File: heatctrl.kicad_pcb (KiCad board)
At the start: 4 copper layers, 57 x 55.5 mm, 6 parts, among them J1 Conn_01x10_Pin, U1 T-Display-S3

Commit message: mcp and t-display-s3
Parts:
- removed J1: Conn_01x10_Pin, Connector_PinSocket_2.54mm:PinSocket_1x10_P2.54mm_Vertical
- removed REF** (x4): MountingHole_3.2mm_M3_Pad, MountingHole:MountingHole_3.2mm_M3_Pad
- added J2: Conn_01x10_Socket, Connector_PinSocket_2.54mm:PinSocket_1x10_P2.54mm_Vertical, F.Cu at (145.4, 74.9)
- added U2: MCP23017_SS, Package_SO:SSOP-28_5.3x10.2mm_P0.65mm, F.Cu at (157.5, 99.1)
- moved U1 20.1 mm to (217.5, 87.6)
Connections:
- U1 pad 1: unconnected-(U1-3v-Pad1) -> +3V3
- U1 pad 11: unconnected-(U1-GND-Pad11) -> GND
- U1 pad 12: unconnected-(U1-5V-Pad12) -> +5V
- U1 pad 17: unconnected-(U1-18-Pad17) -> SCL
- U1 pad 18: Net-(J1-Pin_8) -> SDA
- U1 pad 2: Net-(J1-Pin_2) -> unconnected-(U1-1-Pad2)
- U1 pad 20: Net-(J1-Pin_7) -> unconnected-(U1-16-Pad20)
- U1 pad 24: Net-(J1-Pin_10) -> +3V3
- U1 pad 3: Net-(J1-Pin_3) -> unconnected-(U1-2-Pad3)
- U1 pad 6: Net-(J1-Pin_4) -> unconnected-(U1-11-Pad6)
- U1 pad 7: Net-(J1-Pin_5) -> unconnected-(U1-12-Pad7)
- U1 pad 8: Net-(J1-Pin_6) -> RESET
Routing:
- net Net-(J1-Pin_8): track 82.2 -> 0.00 mm
- net Net-(J1-Pin_7): track 59.6 -> 0.00 mm
- net Net-(J1-Pin_10): track 46.3 -> 0.00 mm
- net Net-(J1-Pin_6): track 10.2 -> 0.00 mm
- net Net-(J1-Pin_5): track 10.2 -> 0.00 mm
- net Net-(J1-Pin_4): track 10.2 -> 0.00 mm
- net Net-(J1-Pin_3): track 10.0 -> 0.00 mm
- net Net-(J1-Pin_2): track 10.0 -> 0.00 mm
- removed copper zone on F.Cu, net GND
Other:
- board outline removed
- board text removed: "AC1"
- board text removed: "AC2"
- board text removed: "AC3"
- board text removed: "AC4"
- board text removed: "AC5"
- board text removed: "AC6"
- board text removed: "AC7"
- board text removed: "GND"
- board text removed: "Heat Controller"
- board text removed: "V1.0 Heiko Vogeler 2026-01-07"

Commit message: start pcb
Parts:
- added D1: Yellow, PCM_JLCPCB:D_0805, F.Cu at (196.2, 77.8)
- added D7: Red, PCM_JLCPCB:D_0805, F.Cu at (200.7, 77.8)
- added J1: Conn_01x10_Socket, Connector_PinSocket_2.54mm:PinSocket_1x10_P2.54mm_Vertical, F.Cu at (168.3, 81.3)
- added R1: 470, Resistor_SMD:R_0603_1608Metric, F.Cu at (196.2, 81.7)
- added R11: 470, Resistor_SMD:R_0603_1608Metric, F.Cu at (200.7, 81.7)
- moved J2 42.5 mm to (145.4, 117.5)
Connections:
- J2 pad 1: unconnected-(J2-Pin_1-Pad1) -> +5V
- J2 pad 10: unconnected-(J2-Pin_10-Pad10) -> GND
- J2 pad 2: unconnected-(J2-Pin_2-Pad2) -> Net-(J2-Pin_2)
- J2 pad 3: unconnected-(J2-Pin_3-Pad3) -> Net-(J2-Pin_3)
- J2 pad 4: unconnected-(J2-Pin_4-Pad4) -> Net-(J2-Pin_4)
- J2 pad 5: unconnected-(J2-Pin_5-Pad5) -> Net-(J2-Pin_5)
- J2 pad 6: unconnected-(J2-Pin_6-Pad6) -> Net-(J2-Pin_6)
- J2 pad 7: unconnected-(J2-Pin_7-Pad7) -> Net-(J2-Pin_7)
- J2 pad 8: unconnected-(J2-Pin_8-Pad8) -> Net-(J2-Pin_8)
- J2 pad 9: unconnected-(J2-Pin_9-Pad9) -> Net-(J2-Pin_9)
- U1 pad 3: unconnected-(U1-2-Pad3) -> Net-(U1-2)
- U1 pad 4: unconnected-(U1-3-Pad4) -> Net-(U1-3)
- U2 pad 1: unconnected-(U2-GPB0-Pad1) -> Net-(J2-Pin_2)
- U2 pad 2: unconnected-(U2-GPB1-Pad2) -> Net-(J2-Pin_3)
- U2 pad 21: unconnected-(U2-GPA0-Pad21) -> Net-(J1-Pin_2)
- U2 pad 22: unconnected-(U2-GPA1-Pad22) -> Net-(J1-Pin_3)
- U2 pad 23: unconnected-(U2-GPA2-Pad23) -> Net-(J1-Pin_4)
- U2 pad 24: unconnected-(U2-GPA3-Pad24) -> Net-(J1-Pin_5)
- U2 pad 25: unconnected-(U2-GPA4-Pad25) -> Net-(J1-Pin_6)
- U2 pad 26: unconnected-(U2-GPA5-Pad26) -> Net-(J1-Pin_7)
- U2 pad 27: unconnected-(U2-GPA6-Pad27) -> Net-(J1-Pin_8)
- U2 pad 28: unconnected-(U2-GPA7-Pad28) -> Net-(J1-Pin_9)
- U2 pad 3: unconnected-(U2-GPB2-Pad3) -> Net-(J2-Pin_4)
- U2 pad 4: unconnected-(U2-GPB3-Pad4) -> Net-(J2-Pin_5)
- U2 pad 5: unconnected-(U2-GPB4-Pad5) -> Net-(J2-Pin_6)
- U2 pad 6: unconnected-(U2-GPB5-Pad6) -> Net-(J2-Pin_7)
- U2 pad 7: unconnected-(U2-GPB6-Pad7) -> Net-(J2-Pin_8)
- U2 pad 8: unconnected-(U2-GPB7-Pad8) -> Net-(J2-Pin_9)
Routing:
- net +5V: track 0.00 -> 213.0 mm
- net RESET: track 0.00 -> 53.4 mm
- net SDA: track 0.00 -> 40.2 mm
- net SCL: track 0.00 -> 38.7 mm
- net GND: track 0.00 -> 29.2 mm, vias 0 -> 11
- net Net-(U1-3): track 0.00 -> 11.0 mm
- net Net-(U1-2): track 0.00 -> 8.71 mm
- net Net-(D7-Pad2): track 0.00 -> 2.16 mm
- net Net-(D1-Pad2): track 0.00 -> 2.16 mm
- added copper zone on B.Cu, net GND
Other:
- board outline added: 93.3 x 60.3 mm

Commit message: finigh 1 pcb
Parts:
- R1, R11: value 470 -> 220
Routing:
- net +3V3: track 0.00 -> 42.4 mm
- net Net-(J2-Pin_9): track 0.00 -> 18.2 mm
- net Net-(J1-Pin_2): track 0.00 -> 17.6 mm
- net Net-(J2-Pin_8): track 0.00 -> 17.4 mm
- net Net-(J2-Pin_2): track 0.00 -> 17.1 mm
- net Net-(J1-Pin_3): track 0.00 -> 16.8 mm
- net Net-(J2-Pin_7): track 0.00 -> 16.6 mm
- net Net-(J1-Pin_9): track 0.00 -> 16.5 mm
- net Net-(J2-Pin_3): track 0.00 -> 16.3 mm
- net Net-(J1-Pin_4): track 0.00 -> 16.0 mm
- net Net-(J2-Pin_6): track 0.00 -> 15.9 mm
- net Net-(J1-Pin_8): track 0.00 -> 15.7 mm
- net Net-(J2-Pin_4): track 0.00 -> 15.5 mm
- net Net-(J1-Pin_5): track 0.00 -> 15.2 mm
- net Net-(J2-Pin_5): track 0.00 -> 15.1 mm
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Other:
- copper layers 4 -> 2

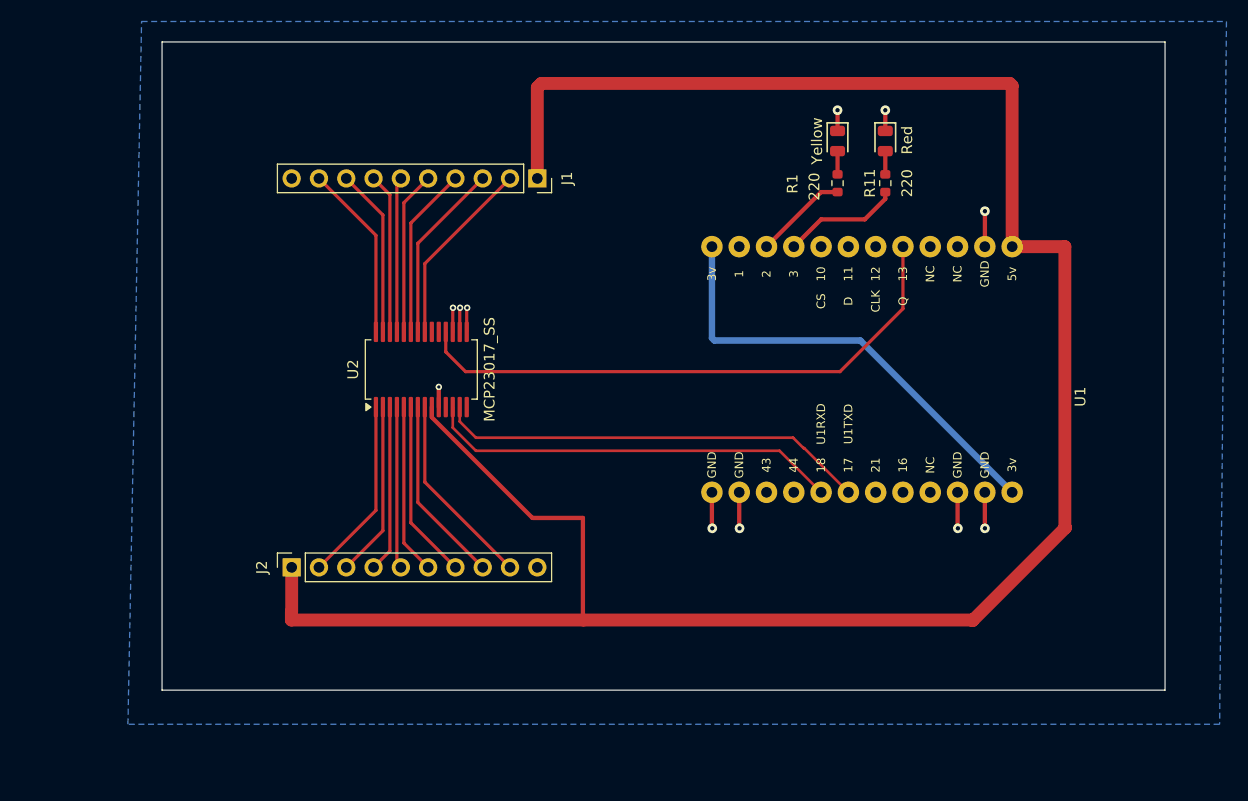
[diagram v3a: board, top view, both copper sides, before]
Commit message: THT components
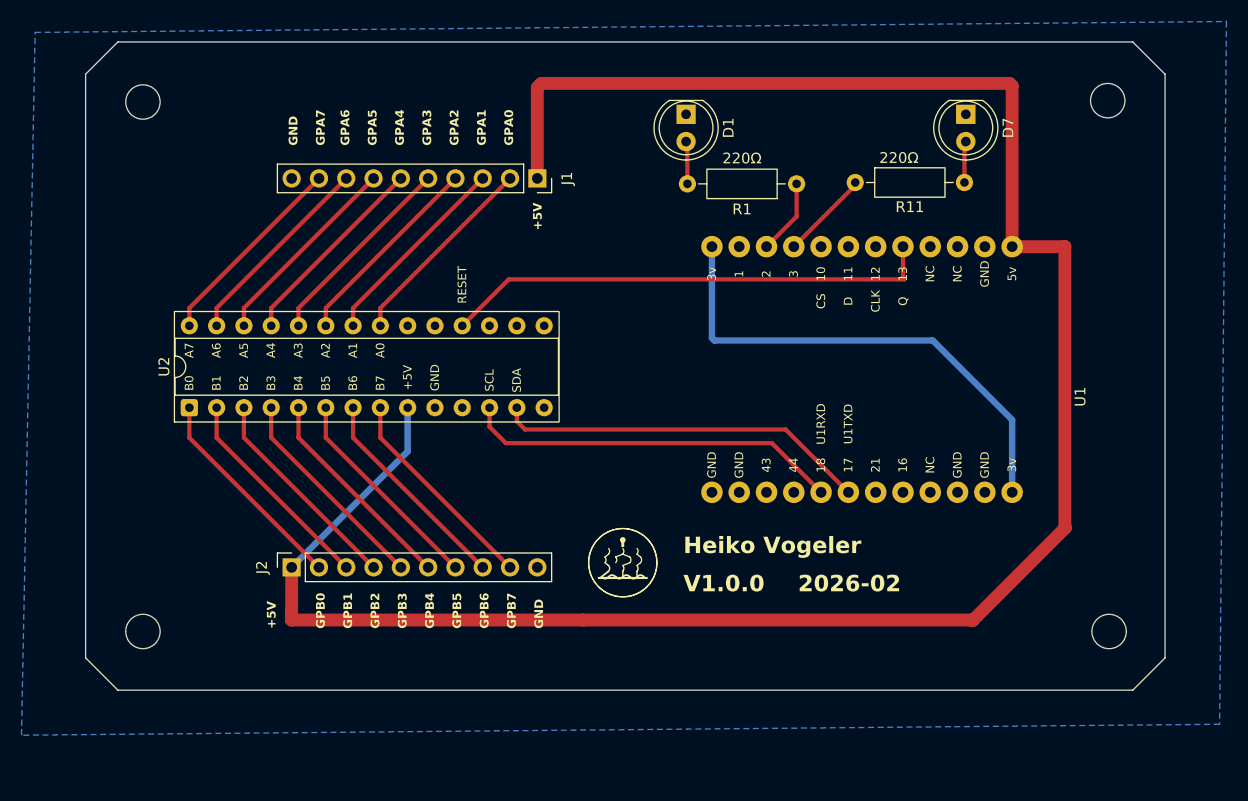
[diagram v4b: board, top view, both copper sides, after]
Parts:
- added REF**: MountingHole_3.2mm_M3, MountingHole:MountingHole_3.2mm_M3, F.Cu at (221.4, 74.0)
- added REF**: MountingHole_3.2mm_M3, MountingHole:MountingHole_3.2mm_M3, F.Cu at (131.6, 123.4)
- added REF**: MountingHole_3.2mm_M3, MountingHole:MountingHole_3.2mm_M3, F.Cu at (221.5, 123.4)
- added REF**: MountingHole_3.2mm_M3, MountingHole:MountingHole_3.2mm_M3, F.Cu at (131.6, 74.2)
- D1, D7: footprint PCM_JLCPCB:D_0805 -> LED_THT:LED_D5.0mm
- R1, R11: value 220 -> 220Ω; footprint Resistor_SMD:R_0603_1608Metric -> Resistor_THT:R_Axial_DIN0207_L6.3mm_D2.5mm_P10.16mm_Horizontal
- U2: footprint Package_SO:SSOP-28_5.3x10.2mm_P0.65mm -> Package_DIP:DIP-28_W7.62mm_Socket
- moved U2 21.9 mm to (135.9, 102.6)
- moved D1 14.3 mm to (182.1, 75.3)
- moved D7 7.90 mm to (208.2, 75.3)
- moved R1 3.81 mm to (192.4, 81.8), turned to 180 degrees
- moved R11 2.79 mm to (197.9, 81.7), turned to 0 degrees
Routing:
- net GND: track 29.2 -> 0.01 mm, vias 11 -> 0
- net +5V: track 207.9 -> 198.8 mm
- net RESET: track 53.4 -> 46.0 mm
- net SDA: track 40.2 -> 34.9 mm
- net Net-(J2-Pin_5): track 15.1 -> 20.4 mm
- net Net-(J1-Pin_6): track 14.4 -> 19.2 mm
- net Net-(J2-Pin_4): track 15.5 -> 19.9 mm
- net Net-(J2-Pin_6): track 15.9 -> 19.9 mm
- net +3V3: track 42.4 -> 46.3 mm
- net Net-(J1-Pin_7): track 14.9 -> 18.7 mm
- net Net-(J2-Pin_3): track 16.3 -> 19.9 mm
- net SCL: track 38.7 -> 35.2 mm
- net Net-(J1-Pin_5): track 15.2 -> 18.7 mm
- net Net-(J2-Pin_7): track 16.6 -> 19.9 mm
- net Net-(J1-Pin_8): track 15.7 -> 18.7 mm
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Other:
- board size 93.3 x 60.3 mm -> 100.5 x 60.3 mm
- board text added: "${COMPANY}"
- board text added: "${REVISION}"
- board text added: "+5V"
- board text added: "2026-02"
- board text added: "A0"
- board text added: "A1"
- board text added: "A2"
- board text added: "A3"
- board text added: "A4"
- board text added: "A5"
- board text added: "A6"
- board text added: "A7"
- board text added: "B0"
- board text added: "B1"
- board text added: "B2"
- board text added: "B3"
- board text added: "B4"
- board text added: "B5"
- board text added: "B6"
- board text added: "B7"
- board text added: "GND"
- board text added: "GPA0"
- board text added: "GPA1"
- board text added: "GPA2"
- board text added: "GPA3"
- board text added: "GPA4"
- board text added: "GPA5"
- board text added: "GPA6"
- board text added: "GPA7"
- board text added: "GPB0"
- board text added: "GPB1"
- board text added: "GPB2"
- board text added: "GPB3"
- board text added: "GPB4"
- board text added: "GPB5"
- board text added: "GPB6"
- board text added: "GPB7"
- board text added: "RESET"
- board text added: "SCL"
- board text added: "SDA"

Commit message: new boards
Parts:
- removed U2: MCP23017_SS, Package_DIP:DIP-28_W7.62mm_Socket
- added R2: 4.7k, Resistor_SMD:R_0603_1608Metric, F.Cu at (204.2, 120.5)
- added R3: 4.7k, Resistor_SMD:R_0603_1608Metric, F.Cu at (204.2, 118.7)
- D1, D7: footprint LED_THT:LED_D5.0mm -> LED_SMD:LED_0805_2012Metric
- R1, R11: value 220Ω -> 220; footprint Resistor_THT:R_Axial_DIN0207_L6.3mm_D2.5mm_P10.16mm_Horizontal -> Resistor_SMD:R_0603_1608Metric
- moved D7 27.1 mm to (181.6, 80.8)
- moved R1 16.9 mm to (175.8, 84.5), turned to 90 degrees
- moved R11 16.5 mm to (181.6, 84.5), turned to 90 degrees
- moved D1 8.41 mm to (175.8, 80.8)
- moved J2 2.54 mm to (145.4, 120.0)
- moved REF**1 2.54 mm to (221.4, 76.6)
- moved J1 2.54 mm to (168.3, 83.8)
- moved REF**2 2.54 mm to (131.6, 76.7)
- moved REF**3 2.54 mm to (221.5, 126.0)
- moved REF**4 2.54 mm to (131.6, 126.0)
- moved U1 2.54 mm to (217.5, 90.2)
- renumbered REF** to REF**1, REF** to REF**2, REF** to REF**3, REF** to REF**4
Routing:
- net SCL: track 35.2 -> 47.3 mm
- net +3V3: track 46.3 -> 58.0 mm
- net Net-(U1-2): track 7.00 -> 15.9 mm
- net SDA: track 34.9 -> 43.3 mm
- net Net-(U1-3): track 8.34 -> 12.5 mm
- net GND: track 0.01 -> 3.56 mm, vias 0 -> 2
- net Net-(D1-Pad2): track 3.99 -> 1.91 mm
- net Net-(D7-Pad2): track 3.86 -> 1.91 mm
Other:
- board text added: "Floor Heating System - ${TITLE}"
- board text added: "JLCJLCJLCJLC"
